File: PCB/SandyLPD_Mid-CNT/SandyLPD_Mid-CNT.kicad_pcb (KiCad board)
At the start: 2 copper layers, 49.4 x 61 mm, 45 parts

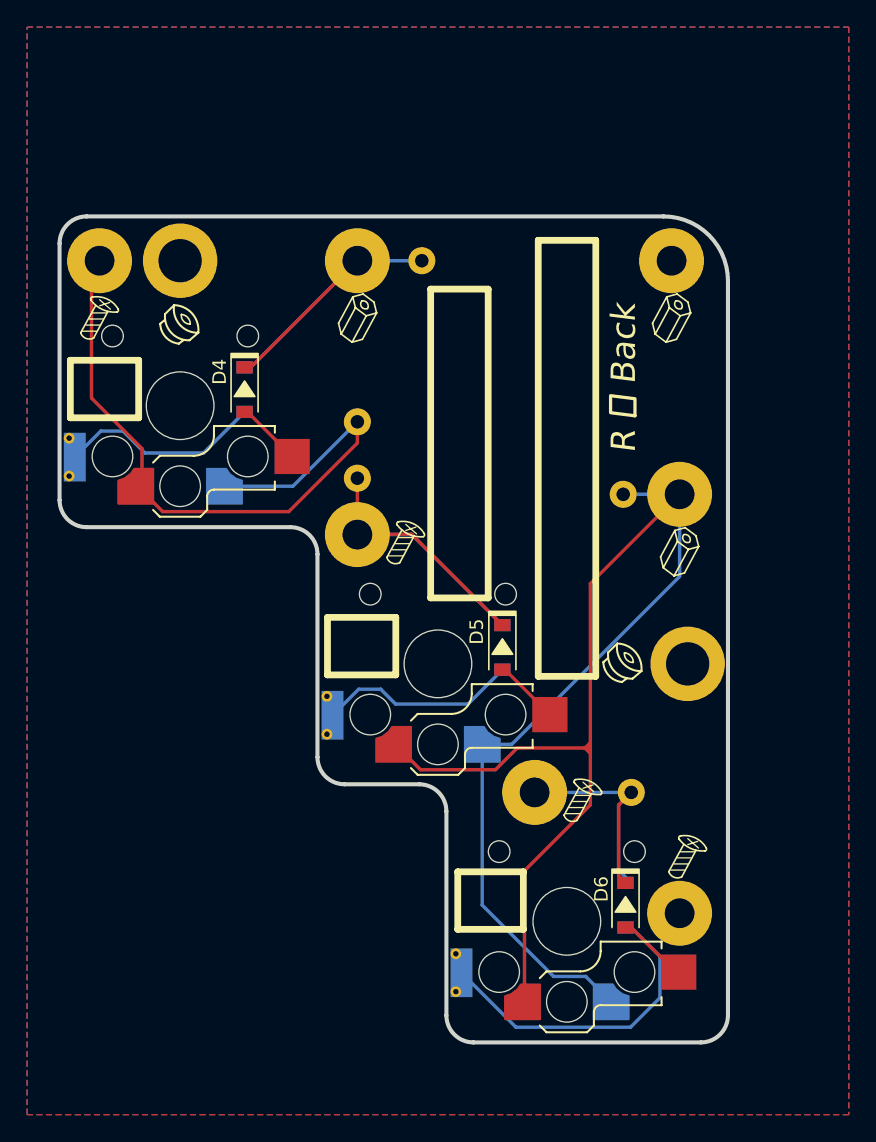
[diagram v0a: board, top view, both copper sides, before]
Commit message: ゴムシート貼り付け指標を調整
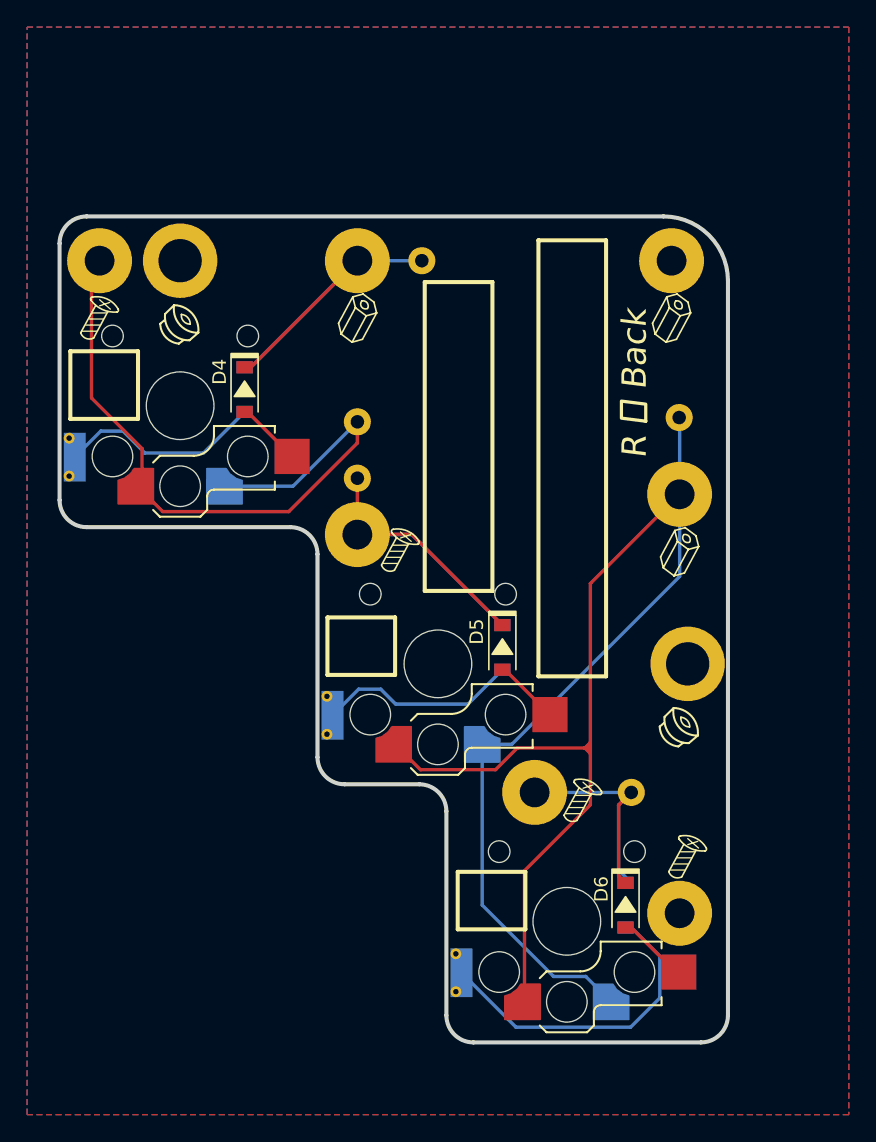
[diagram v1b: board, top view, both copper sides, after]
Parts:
- moved T_C5 7.02 mm to (153.2, 50.5)
- moved REF** 6.33 mm to (153.2, 73.4) (x2)
- moved REF** 0.68 mm to (132.5, 62.9)
- moved REF** 0.47 mm to (132.7, 60.3)
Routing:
- net Mid_col5: track 113.6 -> 115.1 mm
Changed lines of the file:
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@@
 		(locked yes)
 		(layer "F.Cu")
-		(at 149.050722 68.675304)
+		(at 153.217912 73.437806)
 		(property "Reference" "REF**"
 			(at 0 -0.5 0)
@@
 		(locked yes)
 		(layer "F.Cu")
-		(at 132.889966 62.320408)
+		(at 132.496126 62.879764)
 		(property "Reference" "REF**"
 			(at 0 0.5 0)
@@
 	(footprint "locallib:TestPoint_THTPad_D2.0mm_Drill1.0mm"
 		(layer "B.Cu")
-		(at 149.050726 56.173733)
+		(at 153.183435 50.50028)
 		(descr "THT pad as test Point, diameter 2.0mm, hole diameter 1.0mm")
 		(tags "test point THT pad")
@@
 		(locked yes)
 		(layer "B.Cu")
-		(at 149.050722 68.675304 180)
+		(at 153.217913 73.437808 180)
 		(property "Reference" "REF**"
 			(at 0 0.5 0)
@@
 		(fp_arc
 			(start 0.7 3.345415)
-			(mid 0.662237 3.758478)
+			(mid 0.662236 3.758481)
 			(end 0.272339 3.9)
 			(stroke
@@
 		(fp_arc
 			(start 0.7 3.345415)
-			(mid 0.662237 3.758478)
+			(mid 0.662236 3.758481)
 			(end 0.272339 3.9)
 			(stroke
@@
 		(locked yes)
 		(layer "B.Cu")
-		(at 133.06458 60.534467 180)
+		(at 132.670744 60.279764 180)
 		(property "Reference" "REF**"
 			(at 0 -0.5 0)
@@
 		(fp_arc
 			(start 0.7 3.345415)
-			(mid 0.662236 3.758481)
+			(mid 0.662237 3.758478)
 			(end 0.272339 3.9)
 			(stroke
@@
 	)
 	(gr_rect
-		(start 142.770935 37.403444)
-		(end 147.020935 69.623749)
+		(start 142.783435 37.403444)
+		(end 147.783435 69.623749)
 		(stroke
-			(width 0.5)
+			(width 0.3)
 			(type default)
 		)
@@
 	(gr_rect
 		(start 127.220935 65.26903)
-		(end 132.270935 69.51903)
+		(end 132.220935 69.51903)
 		(stroke
-			(width 0.5)
+			(width 0.3)
 			(type default)
 		)
@@
 	)
 	(gr_rect
-		(start 108.220935 46.26903)
-		(end 113.270935 50.51903)
+		(start 108.220935 45.60028)
+		(end 113.220935 50.60028)
 		(stroke
-			(width 0.5)
+			(width 0.3)
 			(type default)
 		)
@@
 	(gr_rect
 		(start 136.795935 84.06903)
-		(end 141.645935 88.31903)
+		(end 141.795935 88.31903)
 		(stroke
-			(width 0.5)
+			(width 0.3)
 			(type default)
 		)
@@
 	)
 	(gr_rect
-		(start 134.820935 41.008878)
-		(end 139.070935 63.829183)
+		(start 134.383435 40.490128)
+		(end 139.383435 63.310433)
 		(stroke
-			(width 0.5)
+			(width 0.3)
 			(type default)
 		)
@@
 	)
 	(gr_rect
-		(start 134.820935 41.008878)
-		(end 139.070935 63.829183)
+		(start 134.383435 40.490128)
+		(end 139.383435 63.310433)
 		(stroke
-			(width 0.5)
+			(width 0.3)
 			(type default)
 		)
@@
 	(gr_rect
 		(start 127.195935 65.26903)
-		(end 132.245935 69.51903)
+		(end 132.195935 69.51903)
 		(stroke
-			(width 0.5)
+			(width 0.3)
 			(type default)
 		)
@@
 	)
 	(gr_rect
-		(start 142.770935 37.403444)
-		(end 147.020935 69.623749)
+		(start 142.783435 37.403444)
+		(end 147.783435 69.623749)
 		(stroke
-			(width 0.5)
+			(width 0.3)
 			(type default)
 		)
@@
 	(gr_rect
 		(start 136.820935 84.06903)
-		(end 141.670935 88.31903)
+		(end 141.820935 88.31903)
 		(stroke
-			(width 0.5)
+			(width 0.3)
 			(type default)
 		)
@@
 	)
 	(gr_rect
-		(start 108.195935 46.26903)
-		(end 113.245935 50.51903)
+		(start 108.195935 45.60028)
+		(end 113.195935 50.60028)
 		(stroke
-			(width 0.5)
+			(width 0.3)
 			(type default)
 		)
@@
 	)
 	(gr_text "L 左 Back"
-		(at 149.183435 47.50028 90)
+		(at 149.983435 47.90028 90)
 		(layer "B.SilkS" knockout)
 		(effects
@@
 	)
 	(gr_text "#SandyLP_Duo DN0010"
-		(at 140.920935 36.11903 90)
+		(at 141.183435 36.11903 90)
 		(layer "B.SilkS")
 		(effects
@@
 	)
 	(gr_text "R 右 Back"
-		(at 149.083435 47.60028 90)
+		(at 149.883435 48.00028 90)
 		(layer "F.SilkS" knockout)
 		(effects
@@
 	)
 	(segment
+		(start 153.217917 56.173733)
+		(end 153.217917 50.534762)
+		(width 0.25)
+		(layer "B.Cu")
+		(net 9)
+	)
+	(segment
 		(start 138.633435 86.53153)
 		(end 143.902185 91.80028)
@@
 	)
 	(segment
+		(start 153.217917 50.534762)
+		(end 153.183435 50.50028)
+		(width 0.25)
+		(layer "B.Cu")
+		(net 9)
+	)
+	(segment
 		(start 140.810085 74.65032)
 		(end 138.633435 74.65032)
@@
 		(width 0.25)
 		(layer "B.Cu")
-		(net 9)
-	)
-	(segment
-		(start 153.217917 56.173733)
-		(end 149.050726 56.173733)
-		(width 0.25)
-		(layer "B.Cu")
